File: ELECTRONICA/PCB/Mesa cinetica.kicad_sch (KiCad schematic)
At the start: 0 parts

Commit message: Estructura inicial
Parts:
- added J1: OLED, symbol Connector:Conn_01x08_Pin
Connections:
- new net +3V3: J1.2 (Pin_2)
- new net BL_BACKLIGH_PWM: J1.8 (Pin_8)
- new net CS_CHIP_SELECT: J1.7 (Pin_7)
- new net DC_DATA_COMMAND: J1.6 (Pin_6)
- new net GND: J1.1 (Pin_1)
- new net RESET_OLED: J1.5 (Pin_5)
- new net SCK_SPI_CLOCK: J1.3 (Pin_3)
- new net SDA_MOSI_SPI: J1.4 (Pin_4)

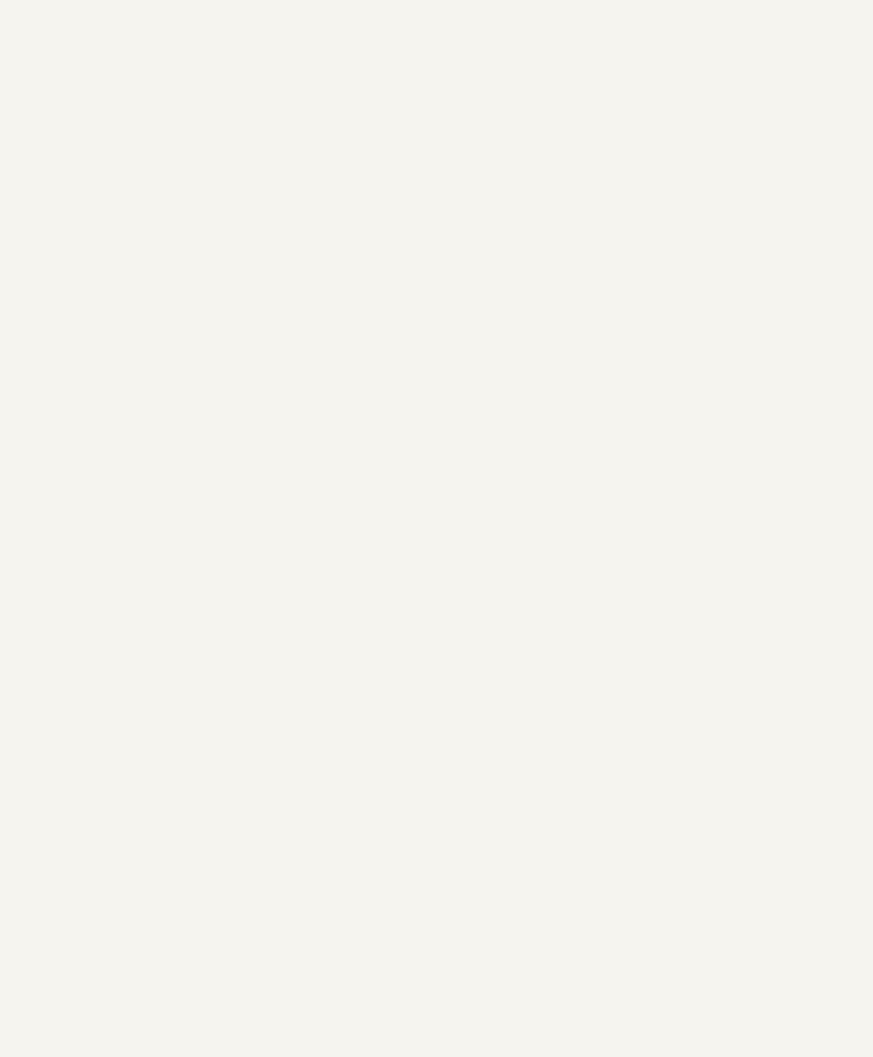
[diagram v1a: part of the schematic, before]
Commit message: El módulo mp3 ya recibe comandos y responde
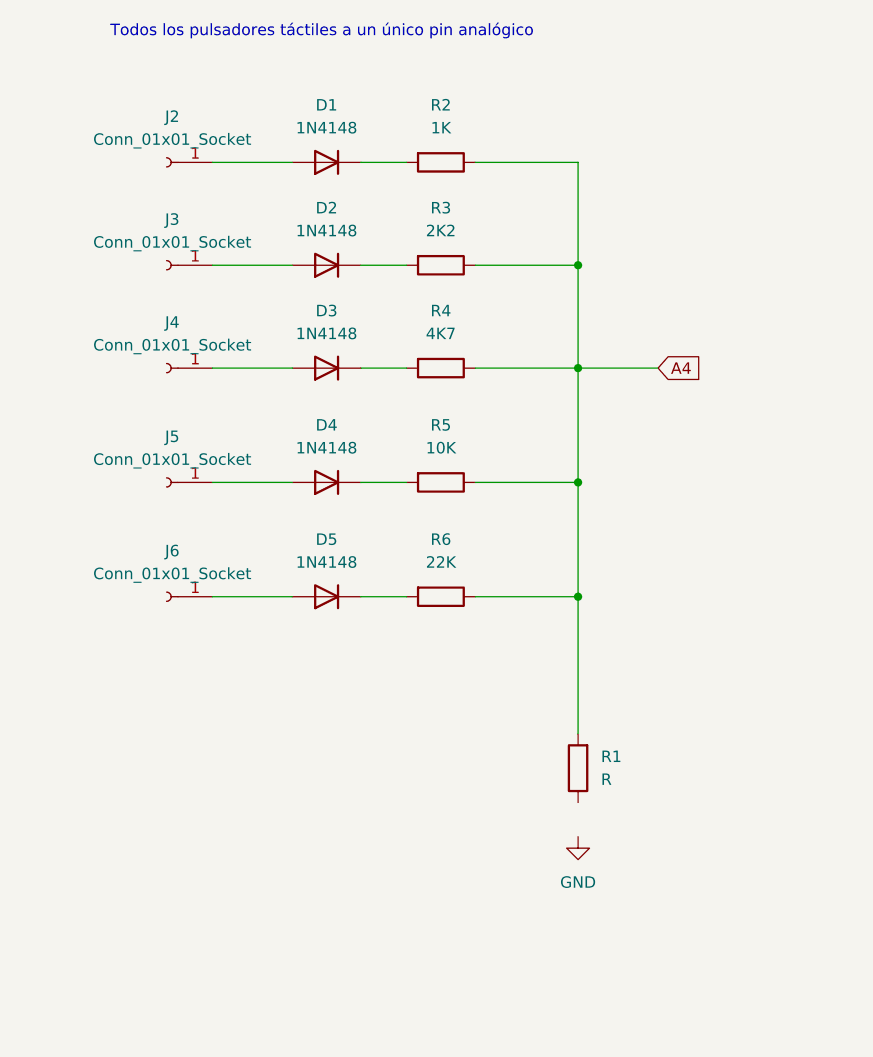
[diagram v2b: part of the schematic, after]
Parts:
- added D1, D2, D3, D4, D5: 1N4148, Diode_THT:D_DO-35_SOD27_P7.62mm_Horizontal, symbol Diode:1N4148
- added J2, J3, J4, J5, J6: Conn_01x01_Socket, symbol Connector:Conn_01x01_Socket
- added R1: R, symbol Device:R
- added R2: 1K, symbol Device:R
- added R3: 2K2, symbol Device:R
- added R4: 4K7, symbol Device:R
- added R5: 10K, symbol Device:R
- added R6: 22K, symbol Device:R
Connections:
- new net: D2.1 (K), R3.2
- new net: D2.2 (A), J3.1 (Pin_1)
- new net: D1.1 (K), R2.2
- new net: D5.1 (K), R6.2
- new net: D5.2 (A), J6.1 (Pin_1)
- new net: D4.1 (K), R5.2
- new net: D4.2 (A), J5.1 (Pin_1)
- new net: D3.1 (K), R4.2
- new net: D3.2 (A), J4.1 (Pin_1)
- new net: D1.2 (A), J2.1 (Pin_1)
- new net A4: R1.2, R2.1, R3.1, R4.1, R5.1, R6.1
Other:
- note added: "Todos los pulsadores táctiles a un único pin analógico"
